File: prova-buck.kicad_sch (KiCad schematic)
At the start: 21 parts, among them J1 Screw_Terminal_01x02, J2 Screw_Terminal_01x02, U1 MPQ9841GL

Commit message: "Updated project"
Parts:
- removed U1: MPQ9841GL, buck_foot_lib:QFN16_3mm_x_4mm, symbol MyLibrary:MPQ9841GL
- added U1: MPQ9842GL, buck_foot_lib:MPQ9842GL-Z, symbol buck_lib:MPQ9842GL
- J1, J2: footprint TerminalBlock:TerminalBlock_bornier-2_P5.08mm -> TerminalBlock_Phoenix:TerminalBlock_Phoenix_MPT-0,5-2-2.54_1x02_P2.54mm_Horizontal
- R3: value 33k -> 169k
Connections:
- net BIAS: now also U1.8 (BIAS)
- net BST: now also U1.11 (BST)
- net En: now also U1.5 (EN)
- net FB: now also U1.15 (FB)
- net FREQ: now also U1.16 (FREQ)
- net GND: now also U1.1 (PHASE), U1.13 (AGND), U1.4 (PGND1), U1.6 (SYNC), U1.9 (PGND2)
- net PG: now also U1.7 (PG)
- net SS: now also U1.14 (SS)
- net VDD: now also U1.2 (VIN)
- net Vcc: now also U1.12 (VCC)
- net SW: no longer names the net of C6.2, L1.1
- net SW: now also U1.10 (SW2)
- no-connect marks 0 -> 1

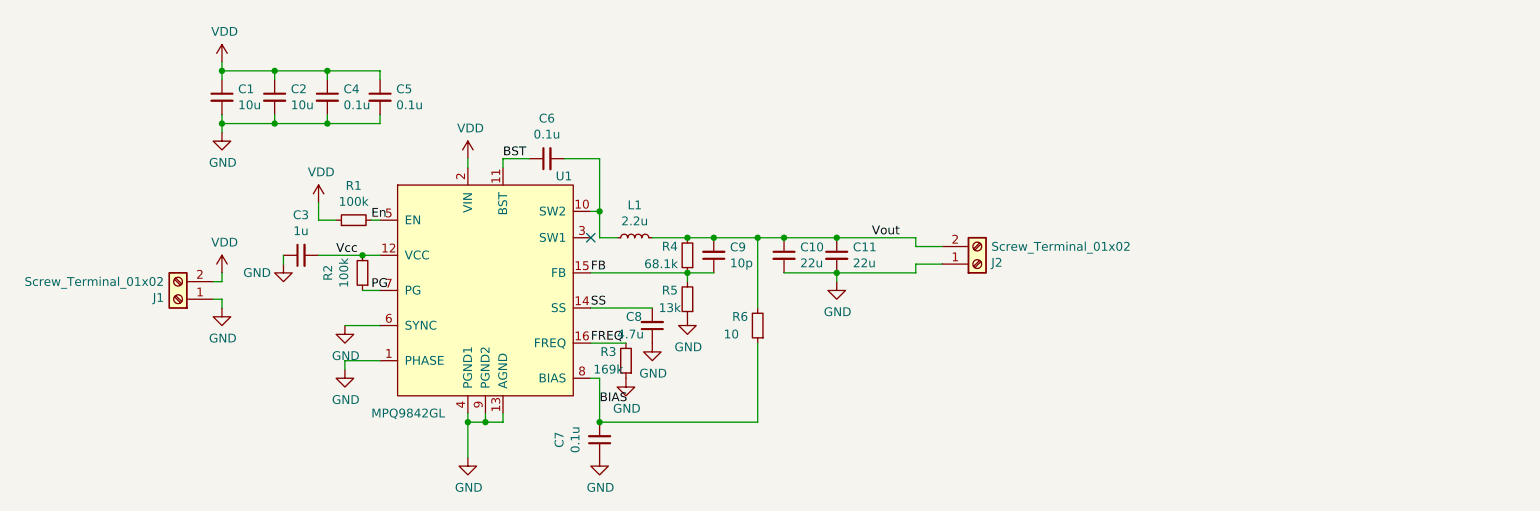
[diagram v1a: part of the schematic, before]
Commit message: "Added Inductor, Buck 3d models"
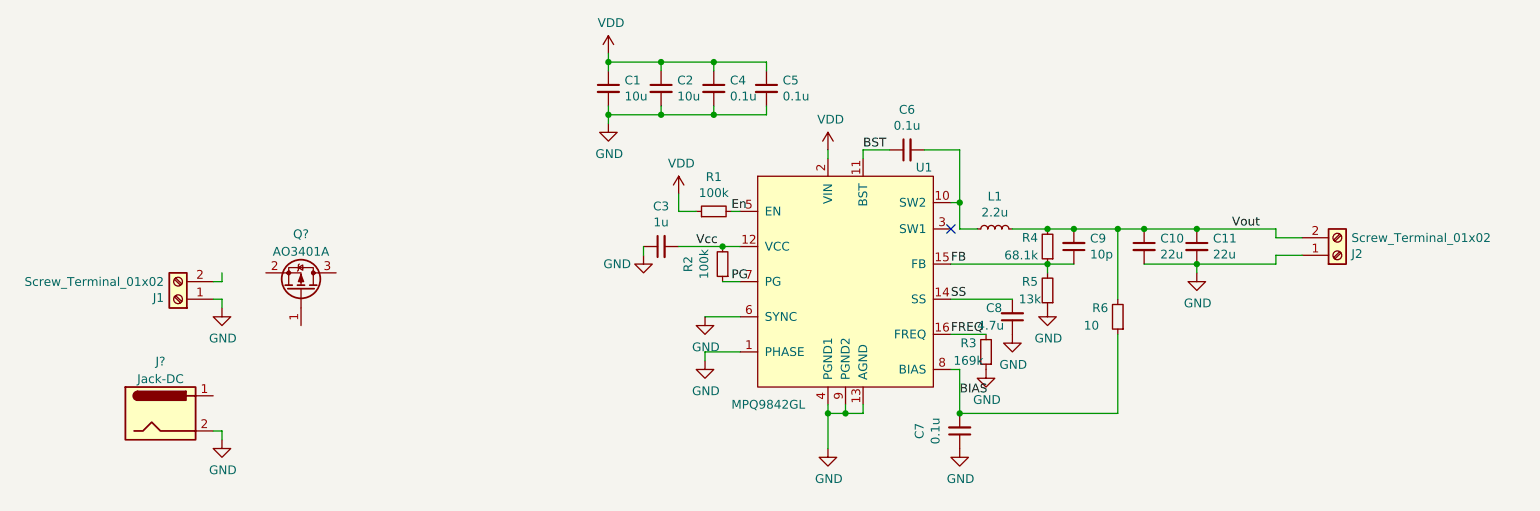
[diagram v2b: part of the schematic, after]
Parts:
- added J?: Jack-DC, symbol Connector:Jack-DC
- added Q?: AO3401A, Package_TO_SOT_SMD:SOT-23, symbol Transistor_FET:AO3401A
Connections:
- net GND: now also J?.2
- net VDD: no longer J1.2 (Pin_2)
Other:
- moved on the sheet: C1, C10, C11, C2, C3, C4, C5, C6, C7, C8, C9, J2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

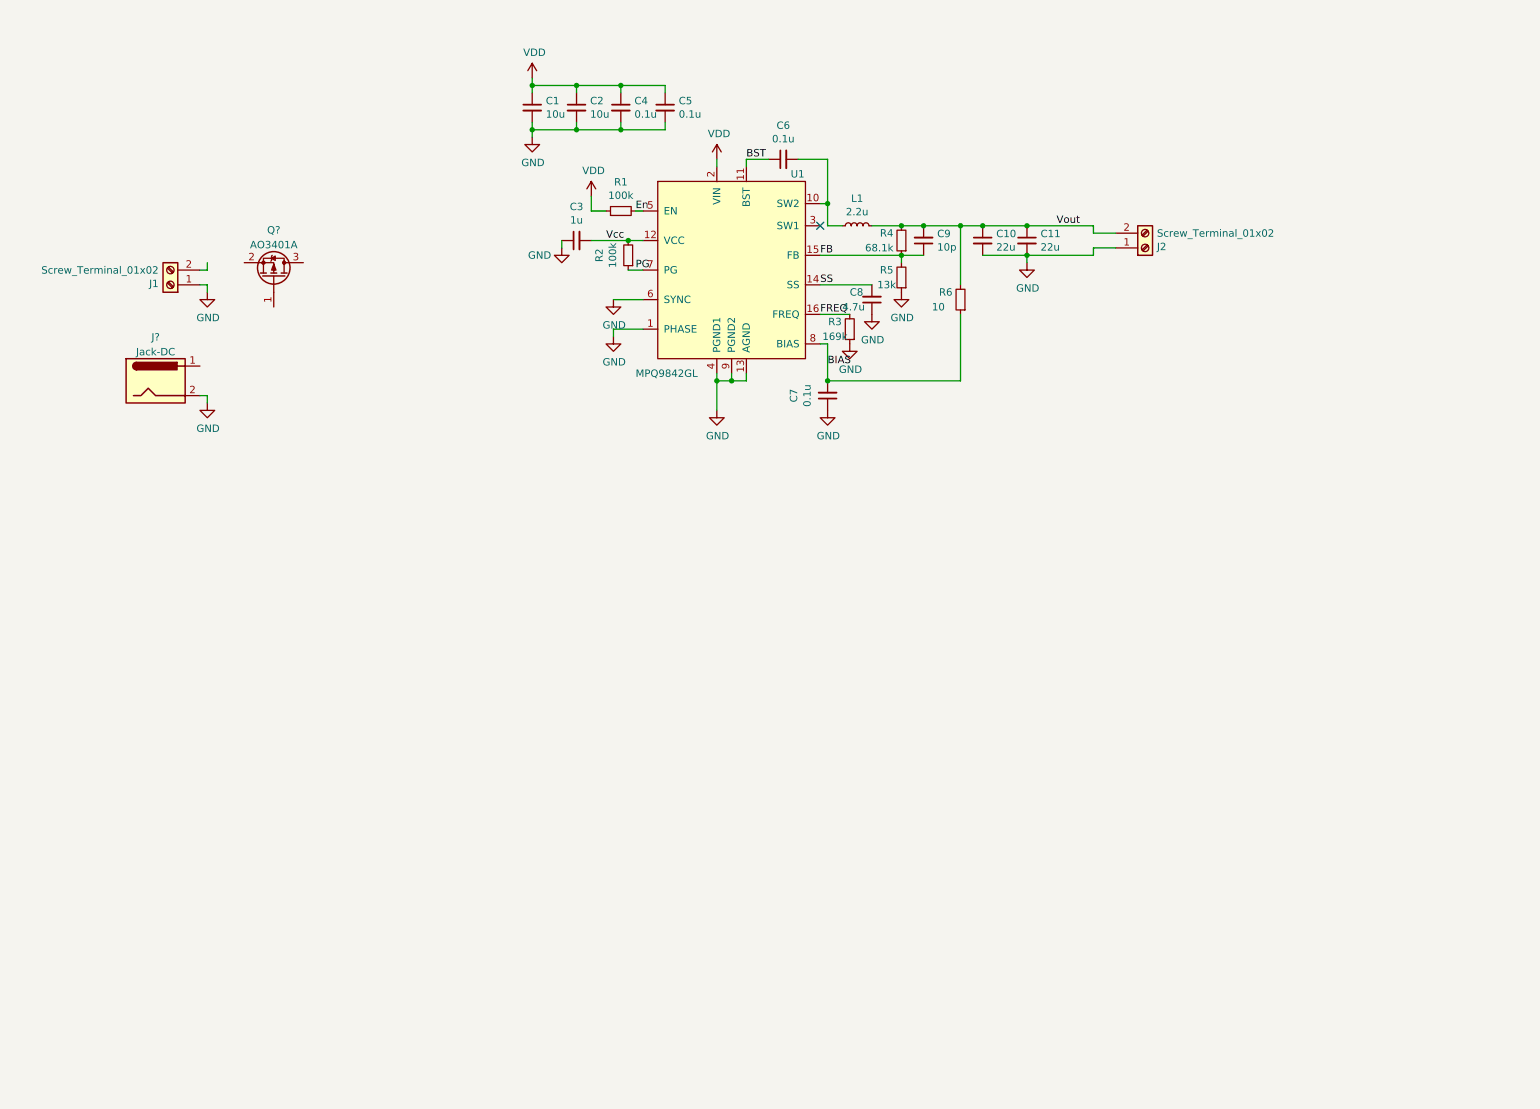
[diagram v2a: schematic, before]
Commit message: " Added power supply selector"
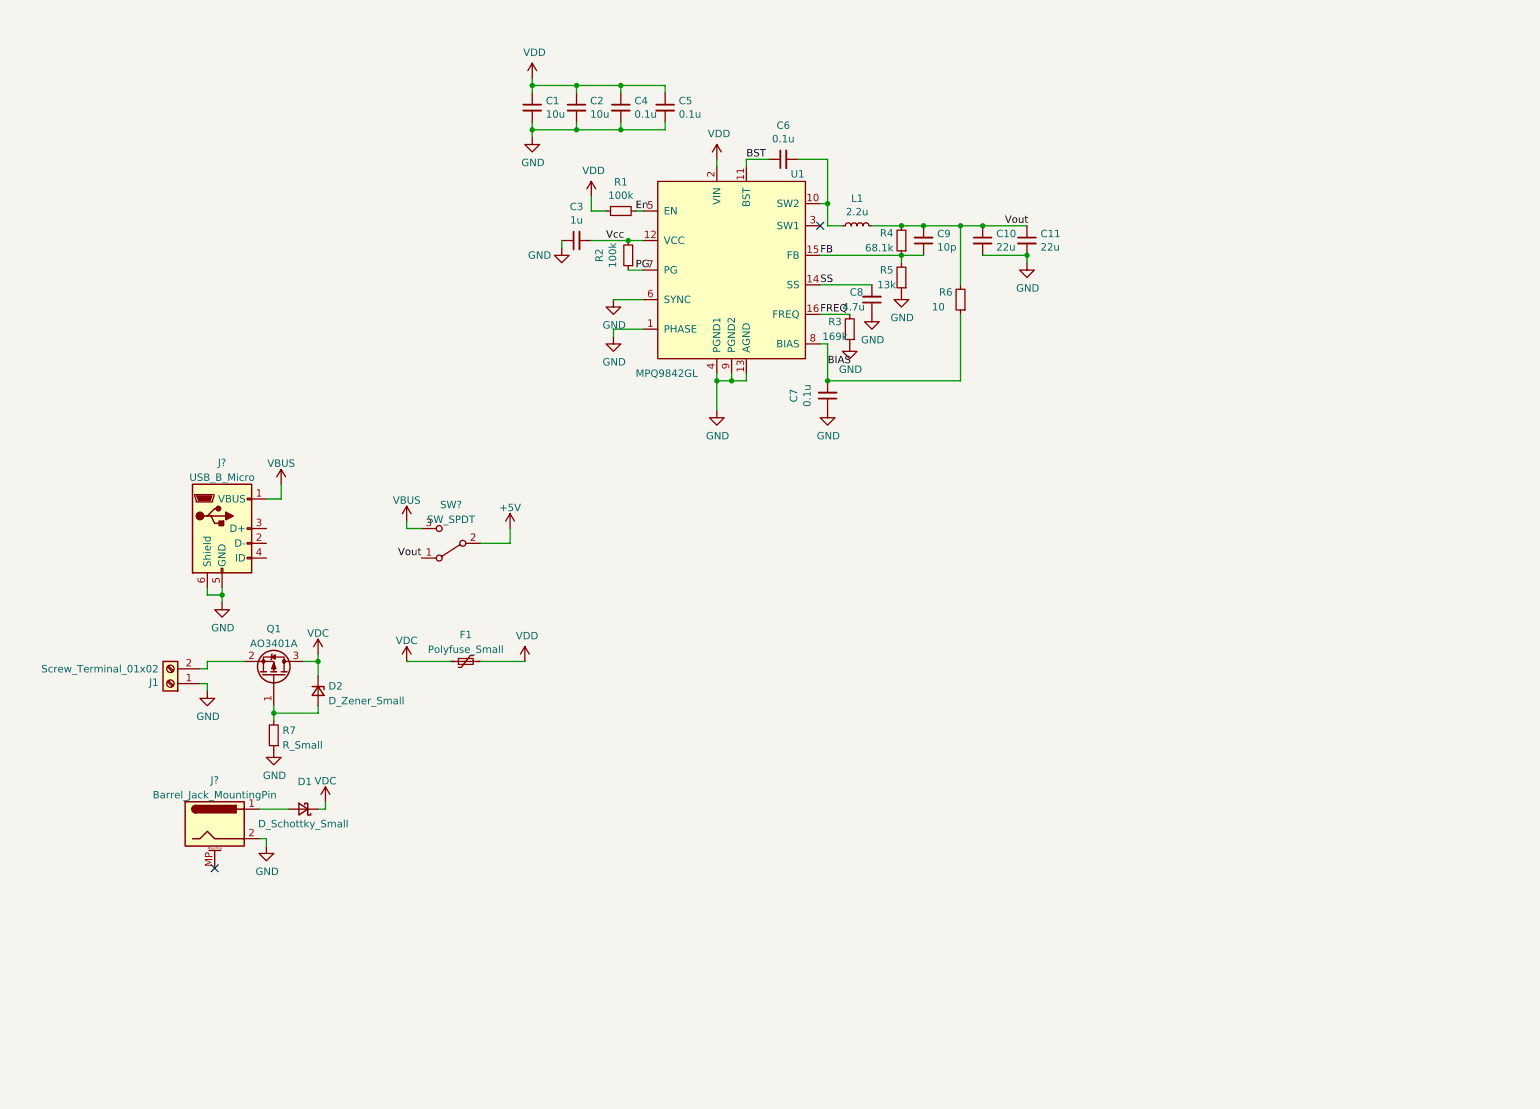
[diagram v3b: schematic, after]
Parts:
- removed J2: Screw_Terminal_01x02, TerminalBlock_Phoenix:TerminalBlock_Phoenix_MPT-0,5-2-2.54_1x02_P2.54mm_Horizontal, symbol Connector:Screw_Terminal_01x02
- removed J?: Jack-DC, symbol Connector:Jack-DC
- added D1: D_Schottky_Small, Diode_SMD:D_SOD-123, symbol Device:D_Schottky_Small
- added D2: D_Zener_Small, Diode_SMD:D_SOD-123, symbol Device:D_Zener_Small
- added F1: Polyfuse_Small, Fuse:Fuse_1812_4532Metric, symbol Device:Polyfuse_Small
- added J?: Barrel_Jack_MountingPin, symbol Connector:Barrel_Jack_MountingPin
- added J?: USB_B_Micro, symbol Connector:USB_B_Micro
- added R7: R_Small, Resistor_SMD:R_0603_1608Metric, symbol Device:R_Small
- added SW?: SW_SPDT, symbol Switch:SW_SPDT
- gave numbers to parts that had none: 1
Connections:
- net GND: now also J?.2, J?.5 (GND), J?.6 (Shield), R7.1
- net VDD: now also F1.2
- net Vout: now also SW?.1 (A)
- net at J1.2 (Pin_2): now also Q1.2 (S)
- net at Q1.1 (G): now also D2.2 (A), R7.2
- net VDC: now reaches Q1.3 (D)
- net VDC: now also D1.1 (K), D2.1 (K), F1.1
- new net: D1.2 (A), J?.1
- new net +5V: SW?.2 (B)
- new net VBUS: J?.1 (VBUS), SW?.3 (C)
- no-connect marks 1 -> 2
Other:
- moved on the sheet: J1, Q1

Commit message: "added LDO"
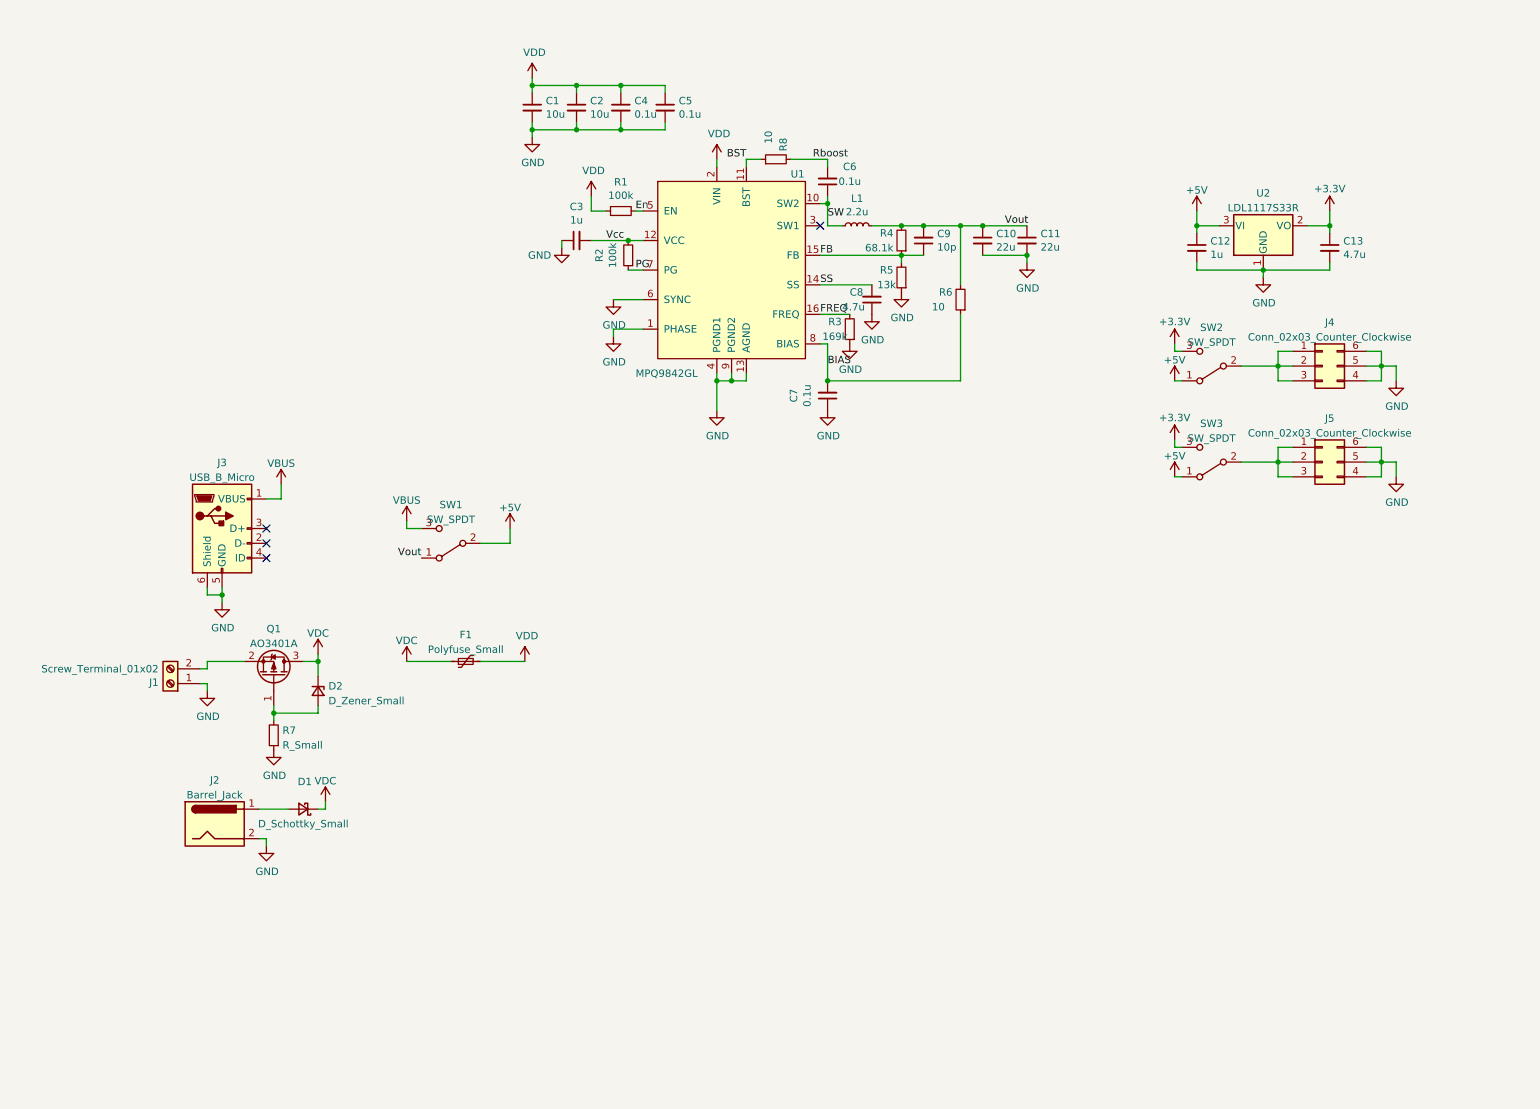
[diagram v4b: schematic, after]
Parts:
- removed J?: Barrel_Jack_MountingPin, symbol Connector:Barrel_Jack_MountingPin
- added C12: 1u, Capacitor_SMD:C_0805_2012Metric, symbol Device:C_Small
- added C13: 4.7u, Capacitor_SMD:C_0805_2012Metric, symbol Device:C_Small
- added J2: Barrel_Jack, Connector_BarrelJack:BarrelJack_Horizontal, symbol Connector:Barrel_Jack
- added J4: Conn_02x03_Counter_Clockwise, Connector_PinHeader_2.54mm:PinHeader_2x03_P2.54mm_Vertical, symbol Connector_Generic:Conn_02x03_Counter_Clockwise
- added J5: Conn_02x03_Counter_Clockwise, Connector_PinSocket_2.54mm:PinSocket_2x03_P2.54mm_Vertical, symbol Connector_Generic:Conn_02x03_Counter_Clockwise
- added R8: 10, Resistor_SMD:R_0402_1005Metric, symbol Device:R_Small
- added SW2, SW3: SW_SPDT, Connector_PinHeader_2.54mm:PinHeader_1x03_P2.54mm_Vertical, symbol Switch:SW_SPDT
- added U2: LDL1117S33R, Package_TO_SOT_SMD:SOT-223-3_TabPin2, symbol Regulator_Linear:AP1117-33
- C6: footprint Capacitor_SMD:C_0603_1608Metric -> Capacitor_SMD:C_0402_1005Metric
- J1: footprint TerminalBlock_Phoenix:TerminalBlock_Phoenix_MPT-0,5-2-2.54_1x02_P2.54mm_Horizontal -> TerminalBlock_Phoenix:TerminalBlock_Phoenix_PT-1,5-2-3.5-H_1x02_P3.50mm_Horizontal
- J3: renamed from J?; footprint (none) -> Connector_USB:USB_Micro-B_Amphenol_10118194_Horizontal
- SW1: renamed from SW?; footprint (none) -> Button_Switch_SMD:SW_SPDT_PCM12
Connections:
- net +5V: now also C12.1, SW2.1 (A), SW3.1 (A), U2.3 (VI)
- net BST: now also R8.1; no longer C6.1
- net GND: now also C12.2, C13.2, J2.2, J4.4 (Pin_4), J4.5 (Pin_5), J4.6 (Pin_6), J5.4 (Pin_4), J5.5 (Pin_5), J5.6 (Pin_6), U2.1 (GND)
- net SW: now reaches L1.1, U1.10 (SW2)
- net SW: now also C6.1; no longer C6.2
- net at D1.2 (A): now also J2.1
- new net: J4.1 (Pin_1), J4.2 (Pin_2), J4.3 (Pin_3), SW2.2 (B)
- new net: J5.1 (Pin_1), J5.2 (Pin_2), J5.3 (Pin_3), SW3.2 (B)
- new net +3V3: C13.1, SW2.3 (C), SW3.3 (C), U2.2 (VO)
- new net Rboost: C6.2, R8.2
- no-connect marks 2 -> 4
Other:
- moved on the sheet: C6
